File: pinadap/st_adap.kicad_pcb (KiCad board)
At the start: 2 copper layers, 29 x 24 mm, 5 parts, among them J1 Conn_02x07_Odd_Even, J2 Conn_01x05_Socket, J3 Conn_01x05_Socket, J4 Conn_01x05_Socket, J5 Conn_01x03_Socket

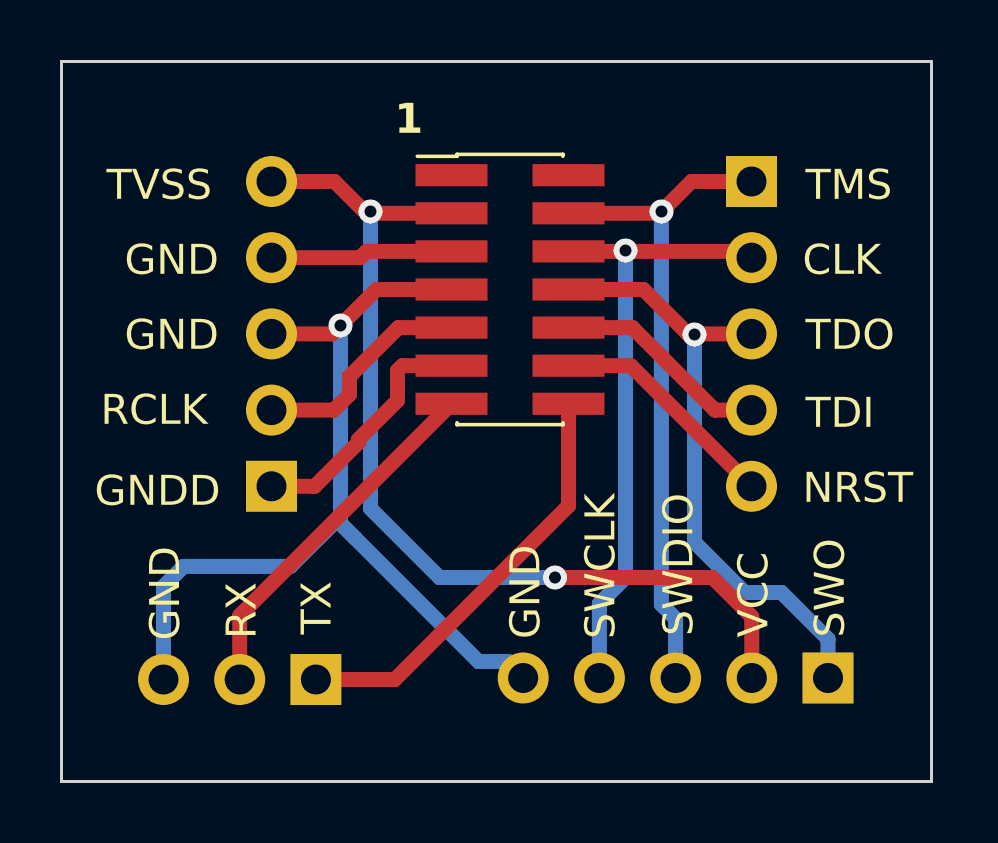
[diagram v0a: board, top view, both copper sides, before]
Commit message: 1.27mm connector with key
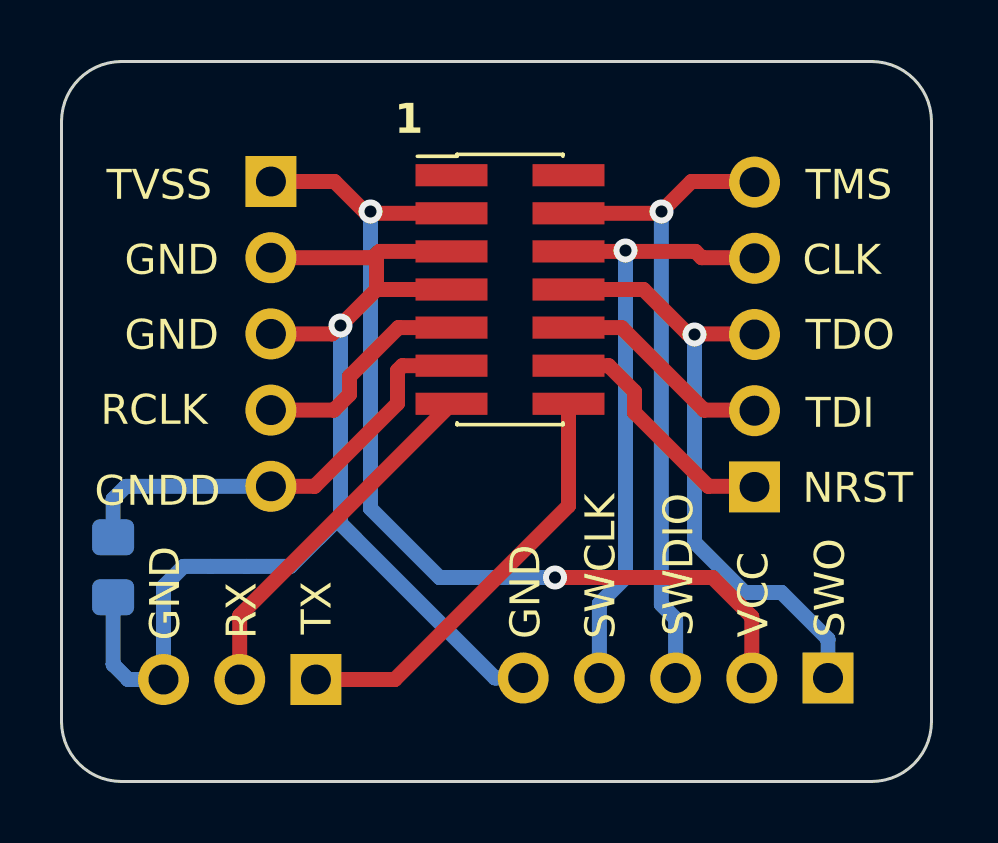
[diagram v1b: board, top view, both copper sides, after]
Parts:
- added R1: 100R, Resistor_SMD:R_0805_2012Metric_Pad1.20x1.40mm_HandSolder, B.Cu at (194.7, 110.9)
- J2, J3: value Conn_01x05_Socket -> Conn_01x05_Pin
- moved J2 10.2 mm to (216.1, 108.2), turned to 0 degrees
- moved J3 10.2 mm to (200.0, 98.0), turned to 180 degrees
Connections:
- J1 pad 5: /GND1 -> /GND
- J1 pad 7: /GND2 -> /GND
- J2 pad 1: /T_JTMS/T_SWDIO -> /T_NRST
- J2 pad 2: /T_JCLK/T_SWCLK -> /T_JTDI/NC
- J2 pad 4: /T_JTDI/NC -> /T_JCLK/T_SWCLK
- J2 pad 5: /T_NRST -> /T_JTMS/T_SWDIO
- J3 pad 1: /GNDDETECT -> /T_VCC
- J3 pad 2: /T_JRCLK -> /GND
- J3 pad 3: /GND2 -> /GND
- J3 pad 4: /GND1 -> /T_JRCLK
- J3 pad 5: /T_VCC -> /GNDDETECT
- J4 pad 5: /GND2 -> /GND
- J5 pad 3: /GND2 -> /GND
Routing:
- net /GND: track 0.00 -> 45.6 mm, vias 0 -> 1
- net /GND2: track 33.4 -> 0.00 mm, vias 1 -> 0
- net /GNDDETECT: track 8.31 -> 15.0 mm
- net /GND1: track 6.09 -> 0.00 mm
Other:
- outline, holes or cut-outs redrawn
